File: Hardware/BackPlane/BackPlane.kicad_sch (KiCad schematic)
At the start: 15 parts, among them J101 CAN, J102 i²c, J103 Power Harness, J104 GPIO, U101 COMPUTER, U102 CARD 0, U103 CARD 1, U104 CARD 2, U105 CARD 3

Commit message: Bump backplane
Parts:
- removed J101: CAN, Connector_JST:JST_EH_B3B-EH-A_1x03_P2.50mm_Vertical, symbol Connector:Conn_01x03_Pin
- removed J103: Power Harness, Connector_JST:JST_EH_B5B-EH-A_1x05_P2.50mm_Vertical, symbol Connector:Conn_01x05_Socket
- added J1, J3: CAN, Connector_Wire:SolderWire-0.5sqmm_1x02_P4.6mm_D0.9mm_OD2.1mm_Relief, symbol Connector:Conn_01x02_Socket
- added J2: Power Harness, Connector_Wire:SolderWire-0.25sqmm_1x03_P4.5mm_D0.65mm_OD2mm_Relief, symbol Connector:Conn_01x03_Socket
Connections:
- net +12V: now also J2.3 (Pin_3)
- net +5V: now also J2.2 (Pin_2)
- net CANH: now also J1.2 (Pin_2), J3.2 (Pin_2)
- net CANL: now also J1.1 (Pin_1), J3.1 (Pin_1)
- net GND: now also J2.1 (Pin_1)
- no-connect marks 25 -> 24

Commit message: Prep for backplane proto
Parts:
- removed H101, H102, H103, H104: MountingHole, MountingHole:MountingHole_3.5mm, symbol Mechanical:MountingHole
- added H1, H2, H3, H4: MountHole, MountingHole:MountingHole_3.5mm_Pad, symbol Mechanical:MountingHole_Pad
- J102: footprint Connector_JST:JST_EH_B3B-EH-A_1x03_P2.50mm_Vertical -> Connector_Wire:SolderWire-0.25sqmm_1x03_P4.5mm_D0.65mm_OD2mm_Relief
- J104: footprint Connector_JST:JST_EH_B5B-EH-A_1x05_P2.50mm_Vertical -> Connector_Wire:SolderWire-0.5sqmm_1x05_P4.6mm_D0.9mm_OD2.1mm_Relief
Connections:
- net GND: now also H1.1, H2.1, H3.1, H4.1
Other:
- moved on the sheet: J1, J2, J3

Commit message: So near to a backplane prototype now
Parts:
- added F1: Fuse, Fuse:Fuseholder_Littelfuse_100_series_5x20mm, symbol Device:Fuse
- U102: value CARD 0 -> CARD 1
- U103: value CARD 1 -> CARD 2
- U104: value CARD 2 -> CARD 3
- U105: value CARD 3 -> CARD 4
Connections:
- net CARD_EN_0 is gone; now on net CARD_EN_1: U101.3 (CARD_EN), U102.3 (CARD_EN)
- net CARD_SEL_0 is gone; now on net CARD_SEL_1: U101.4 (CARD_SEL), U102.4 (CARD_SEL)
- net +12V: now also F1.1; no longer J2.3 (Pin_3)
- net CARD_EN_1: no longer U101.5 (CARD_EN2), U103.3 (CARD_EN)
- net CARD_EN_2: now also U101.5 (CARD_EN2), U103.3 (CARD_EN); no longer U101.7 (CARD_EN3), U104.3 (CARD_EN)
- net CARD_EN_3: now also U101.7 (CARD_EN3), U104.3 (CARD_EN); no longer U101.9 (CARD_EN4), U105.3 (CARD_EN)
- net CARD_SEL_1: no longer U101.6 (CARD_SEL2), U103.4 (CARD_SEL)
- net CARD_SEL_2: now also U101.6 (CARD_SEL2), U103.4 (CARD_SEL); no longer U101.8 (CARD_SEL3), U104.4 (CARD_SEL)
- net CARD_SEL_3: now also U101.8 (CARD_SEL3), U104.4 (CARD_SEL); no longer U101.10 (CARD_SEL4), U105.4 (CARD_SEL)
- new net: F1.2, J2.3 (Pin_3)
- new net CARD_EN_4: U101.9 (CARD_EN4), U105.3 (CARD_EN)
- new net CARD_SEL_4: U101.10 (CARD_SEL4), U105.4 (CARD_SEL)
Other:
- moved on the sheet: J2

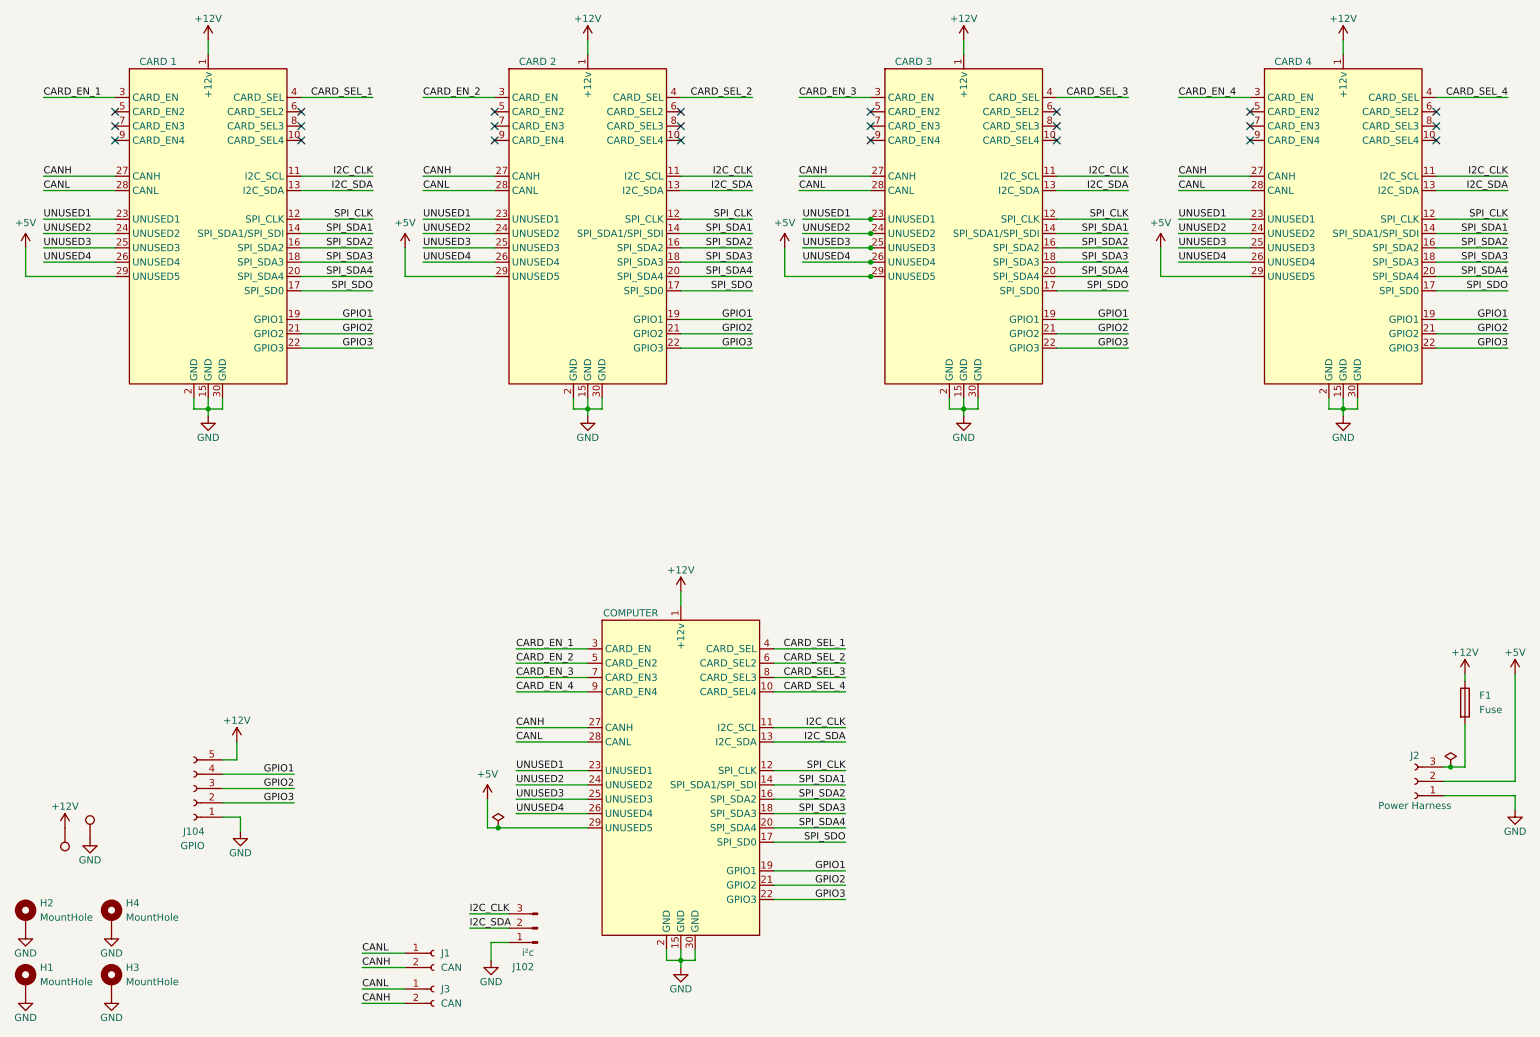
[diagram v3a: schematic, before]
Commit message: Backplane now calls UNUSED5 5v offically
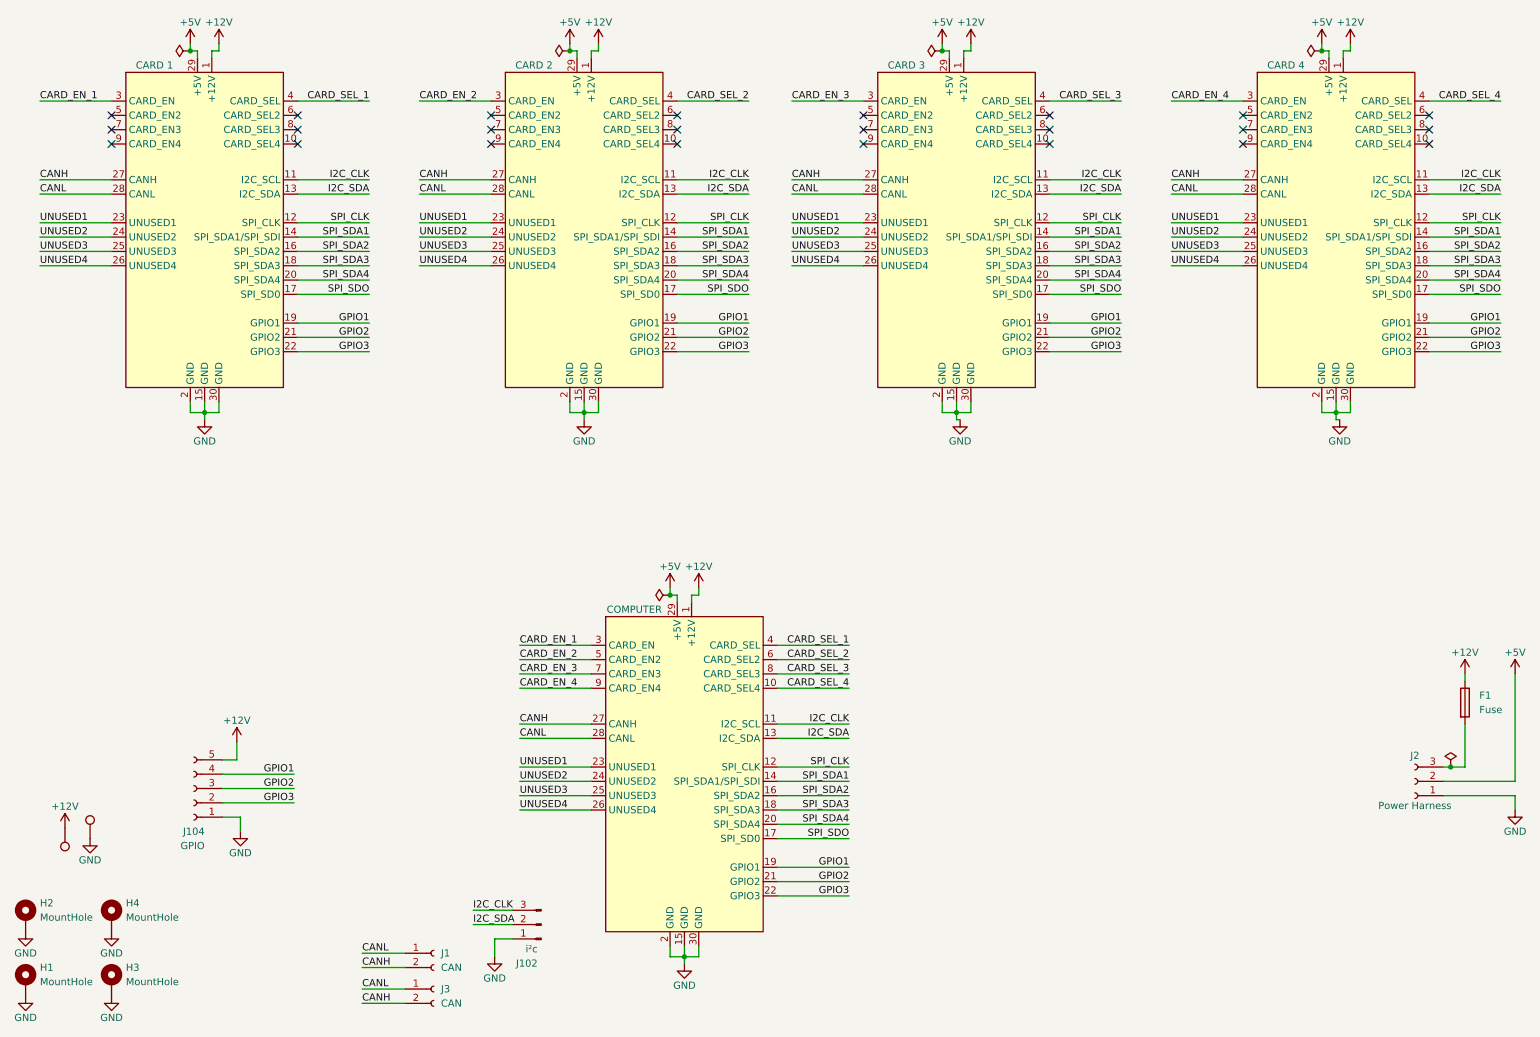
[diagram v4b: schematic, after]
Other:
- moved on the sheet: J102
